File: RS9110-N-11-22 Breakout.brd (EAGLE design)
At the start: 43.2 x 43.2 mm, 13 parts, among them U1 RS9110-N-11-22

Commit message: Add notes about when to populate resistors
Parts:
- R1, R2, R7, R8: value 1k-10k -> 1k-10k (if UART)
- R3: value 3.9k-4.7k -> 3.9k-4.7k (if SPI)
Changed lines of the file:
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@@
 <element name="U1" library="x-io" package="RS9110-N-11-22" value="RS9110-N-11-22" x="23.495" y="27.94" smashed="yes" rot="R90"/>
 <element name="JP1" library="SparkFun-Connectors" package="1X16" value="M16PTH" x="2.54" y="2.54" smashed="yes"/>
-<element name="R1" library="SparkFun-Resistors" package="0603-RES" value="1k-10k" x="22.86" y="16.51" smashed="yes" rot="MR270">
+<element name="R1" library="SparkFun-Resistors" package="0603-RES" value="1k-10k (if UART)" x="22.86" y="16.51" smashed="yes" rot="MR270">
 <attribute name="NAME" x="22.225" y="19.05" size="0.8128" layer="26" font="vector" rot="MR90"/>
 <attribute name="VALUE" x="22.225" y="21.59" size="0.8128" layer="28" font="vector" rot="MR90"/>
 </element>
-<element name="R2" library="SparkFun-Resistors" package="0603-RES" value="1k-10k" x="35.56" y="9.525" smashed="yes" rot="MR270">
+<element name="R2" library="SparkFun-Resistors" package="0603-RES" value="1k-10k (if UART)" x="35.56" y="9.525" smashed="yes" rot="MR270">
 <attribute name="NAME" x="34.925" y="12.065" size="0.8128" layer="26" font="vector" rot="MR90"/>
 <attribute name="VALUE" x="34.925" y="14.605" size="0.8128" layer="28" font="vector" rot="MR90"/>
 </element>
-<element name="R3" library="SparkFun-Resistors" package="0603-RES" value="3.9k-4.7k" x="40.64" y="19.05" smashed="yes" rot="MR270">
+<element name="R3" library="SparkFun-Resistors" package="0603-RES" value="3.9k-4.7k (if SPI)" x="40.64" y="19.05" smashed="yes" rot="MR270">
 <attribute name="NAME" x="40.005" y="21.59" size="0.8128" layer="26" font="vector" rot="MR90"/>
 <attribute name="VALUE" x="40.005" y="24.13" size="0.8128" layer="28" font="vector" rot="MR90"/>
@@
 <attribute name="VALUE" x="12.065" y="15.875" size="0.8128" layer="28" font="vector" rot="MR90"/>
 </element>
-<element name="R7" library="SparkFun-Resistors" package="0603-RES" value="1k-10k" x="17.78" y="15.875" smashed="yes" rot="MR270">
+<element name="R7" library="SparkFun-Resistors" package="0603-RES" value="1k-10k (if UART)" x="17.78" y="15.875" smashed="yes" rot="MR270">
 <attribute name="NAME" x="17.145" y="18.415" size="0.8128" layer="26" font="vector" rot="MR90"/>
 <attribute name="VALUE" x="17.145" y="20.955" size="0.8128" layer="28" font="vector" rot="MR90"/>
 </element>
-<element name="R8" library="SparkFun-Resistors" package="0603-RES" value="1k-10k" x="20.32" y="15.24" smashed="yes" rot="MR270">
+<element name="R8" library="SparkFun-Resistors" package="0603-RES" value="1k-10k (if UART)" x="20.32" y="15.24" smashed="yes" rot="MR270">
 <attribute name="NAME" x="19.685" y="17.78" size="0.8128" layer="26" font="vector" rot="MR90"/>
 <attribute name="VALUE" x="19.685" y="20.32" size="0.8128" layer="28" font="vector" rot="MR90"/>

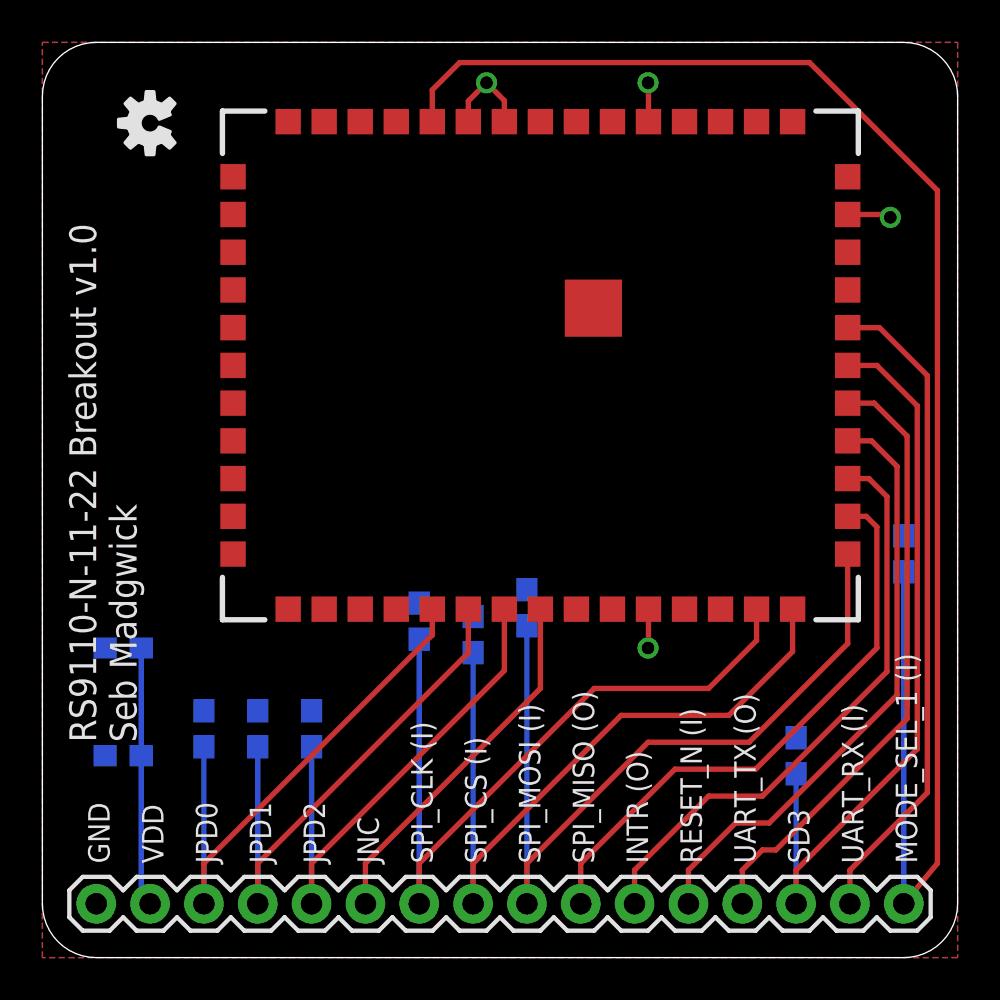
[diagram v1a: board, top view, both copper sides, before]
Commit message: Remove copper from around antenna
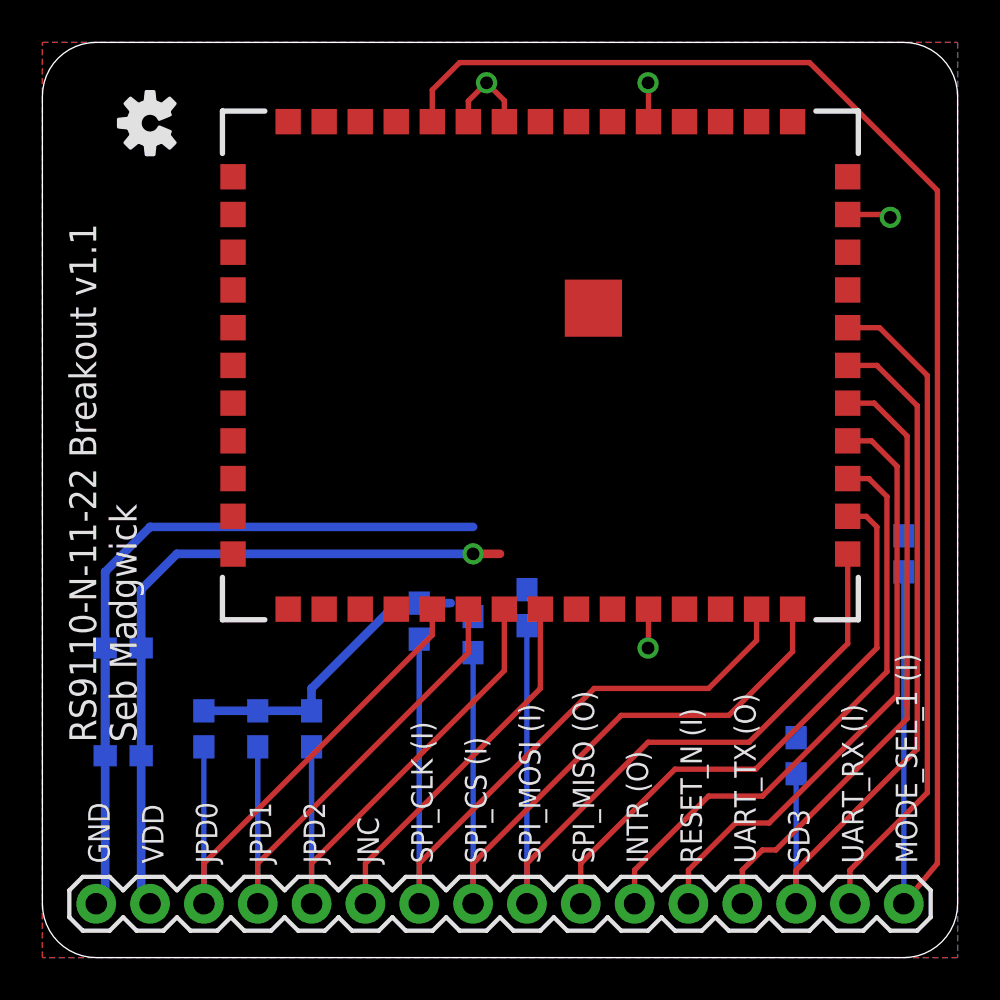
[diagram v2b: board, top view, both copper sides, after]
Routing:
- net GND: track 10.1 -> 63.6 mm
- net VDD: track 12.2 -> 32.6 mm, vias 0 -> 1
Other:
- board text added: "RS9110-N-11-22 Breakout v1.1"
- board text removed: "RS9110-N-11-22 Breakout v1.0"
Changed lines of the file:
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@@
 <setting verticaltext="up"/>
 </settings>
-<grid distance="0.0125" unitdist="inch" unit="inch" style="dots" multiple="1" display="yes" altdistance="0.000004" altunitdist="inch" altunit="inch"/>
+<grid distance="0.05" unitdist="inch" unit="inch" style="dots" multiple="1" display="yes" altdistance="0.000004" altunitdist="inch" altunit="inch"/>
 <layers>
 <layer number="1" name="Top" color="4" fill="1" visible="yes" active="yes"/>
@@
 <layer number="39" name="tKeepout" color="4" fill="11" visible="no" active="yes"/>
 <layer number="40" name="bKeepout" color="1" fill="11" visible="no" active="yes"/>
-<layer number="41" name="tRestrict" color="4" fill="10" visible="no" active="yes"/>
-<layer number="42" name="bRestrict" color="1" fill="10" visible="no" active="yes"/>
+<layer number="41" name="tRestrict" color="4" fill="10" visible="yes" active="yes"/>
+<layer number="42" name="bRestrict" color="1" fill="10" visible="yes" active="yes"/>
 <layer number="43" name="vRestrict" color="2" fill="10" visible="no" active="yes"/>
 <layer number="44" name="Drills" color="7" fill="1" visible="no" active="yes"/>
@@
 <wire x1="40.64" y1="0" x2="43.18" y2="2.54" width="0" layer="20" curve="90"/>
 <wire x1="40.64" y1="43.18" x2="43.18" y2="40.64" width="0" layer="20" curve="-90"/>
-<text x="2.54" y="10.16" size="1.27" layer="121" font="vector" rot="R90">RS9110-N-11-22 Breakout v1.0</text>
+<text x="2.54" y="10.16" size="1.27" layer="121" font="vector" rot="R90">RS9110-N-11-22 Breakout v1.1</text>
 <text x="4.445" y="10.16" size="1.27" layer="121" font="vector" rot="R90">Seb Madgwick</text>
 <text x="3.175" y="4.445" size="1.016" layer="121" font="vector" rot="R90">GND</text>
@@
 <text x="32.385" y="4.445" size="1.016" layer="122" font="vector" rot="MR90">UART_TX (O)</text>
 <text x="24.765" y="4.445" size="1.016" layer="122" font="vector" rot="MR90">SPI_MISO (O)</text>
+<polygon width="0.254" layer="42">
+<vertex x="0" y="0"/>
+<vertex x="19.05" y="0"/>
+<vertex x="19.05" y="43.18"/>
+<vertex x="0" y="43.18"/>
+</polygon>
+<polygon width="0.254" layer="41">
+<vertex x="0" y="0"/>
+<vertex x="19.05" y="0"/>
+<vertex x="19.05" y="43.18"/>
+<vertex x="0" y="43.18"/>
+</polygon>
 </plain>
 <attributes>
@@
 <wire x1="37.995" y1="35.06" x2="39.87" y2="35.06" width="0.254" layer="1"/>
 <wire x1="39.87" y1="35.06" x2="40.005" y2="34.925" width="0.254" layer="1"/>
+<wire x1="7.62" y1="11.645" x2="10.16" y2="11.645" width="0.4064" layer="16"/>
+<wire x1="10.16" y1="11.645" x2="12.7" y2="11.645" width="0.4064" layer="16"/>
+<wire x1="12.7" y1="11.645" x2="12.7" y2="12.7" width="0.4064" layer="16"/>
+<wire x1="12.7" y1="12.7" x2="16.725" y2="16.725" width="0.4064" layer="16"/>
+<wire x1="17.78" y1="16.725" x2="16.725" y2="16.725" width="0.4064" layer="16"/>
+<wire x1="17.78" y1="16.725" x2="19.265" y2="16.725" width="0.4064" layer="16"/>
+<wire x1="2.96" y1="14.605" x2="2.96" y2="9.525" width="0.4064" layer="16"/>
+<wire x1="2.96" y1="9.525" x2="2.96" y2="2.96" width="0.4064" layer="16"/>
+<wire x1="2.96" y1="2.96" x2="2.54" y2="2.54" width="0.4064" layer="16"/>
+<wire x1="2.96" y1="9.525" x2="2.96" y2="18.2" width="0.4064" layer="16"/>
+<wire x1="2.96" y1="18.2" x2="5.08" y2="20.32" width="0.4064" layer="16"/>
+<wire x1="5.08" y1="20.32" x2="20.32" y2="20.32" width="0.4064" layer="16"/>
 </signal>
 <signal name="VDD">
@@
 <contactref element="C1" pad="1"/>
 <contactref element="C2" pad="1"/>
-<wire x1="4.66" y1="9.525" x2="4.66" y2="2.96" width="0.254" layer="16"/>
-<wire x1="4.66" y1="2.96" x2="5.08" y2="2.54" width="0.254" layer="16"/>
-<wire x1="4.66" y1="14.605" x2="4.66" y2="9.525" width="0.254" layer="16"/>
+<wire x1="4.66" y1="14.605" x2="4.66" y2="9.525" width="0.4064" layer="16"/>
+<wire x1="4.66" y1="9.525" x2="4.66" y2="2.96" width="0.4064" layer="16"/>
+<wire x1="4.66" y1="2.96" x2="5.08" y2="2.54" width="0.4064" layer="16"/>
+<wire x1="4.66" y1="14.605" x2="4.66" y2="17.36" width="0.4064" layer="16"/>
+<wire x1="4.66" y1="17.36" x2="6.35" y2="19.05" width="0.4064" layer="16"/>
+<wire x1="6.35" y1="19.05" x2="20.32" y2="19.05" width="0.4064" layer="16"/>
+<via x="20.32" y="19.05" extent="1-16" drill="0.6"/>
+<wire x1="20.32" y1="19.05" x2="21.59" y2="19.05" width="0.4064" layer="1"/>
 </signal>
 <signal name="SPI_MISO">
@@
 </signal>
 </signals>
+<errors>
+</errors>
 </board>
 </drawing>
